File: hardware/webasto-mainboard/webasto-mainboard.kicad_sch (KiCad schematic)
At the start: 15 parts, among them J1 Console FTDI, J2 DEBUG, Q1 DMG2301L, U1 CY15E004J, U2 Pico, U3 LM4040DIM3-3.0

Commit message: Update title block on mainboard, print PDFs
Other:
- company: (none) -> Gavin Hurlbut
- title: Webasto Thermo Top C Replacement Controller -> Webasto Replacement Mainboard (Thermo Top C)
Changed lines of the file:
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@@
   (paper "A4")
   (title_block
-    (title "Webasto Thermo Top C Replacement Controller")
-    (date "2023-01-19")
+    (title "Webasto Replacement Mainboard (Thermo Top C)")
+    (date "2023-01-31")
     (rev "v1.0")
+    (company "Gavin Hurlbut")
   )
   (junction (at 122.301 114.173) (diameter 0) (color 0 0 0 0)

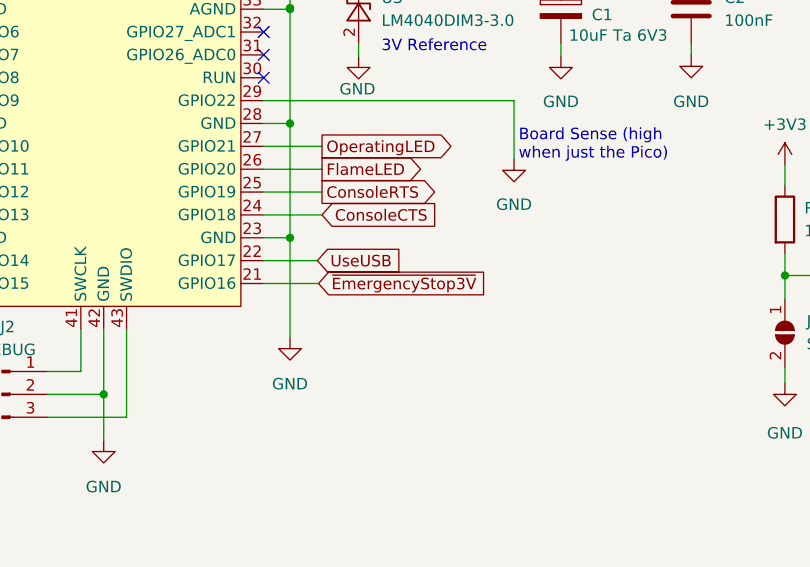
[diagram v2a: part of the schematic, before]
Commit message: Moved emerg. shutdown offboard
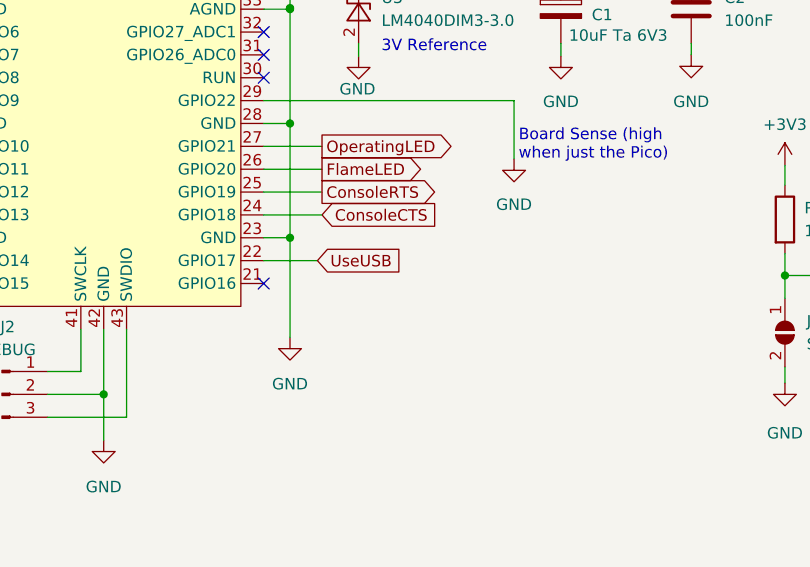
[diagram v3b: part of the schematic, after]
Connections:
- net ~{EmergencyStop3V}: no longer names the net of U2.21 (GPIO16)
- no-connect marks 5 -> 6

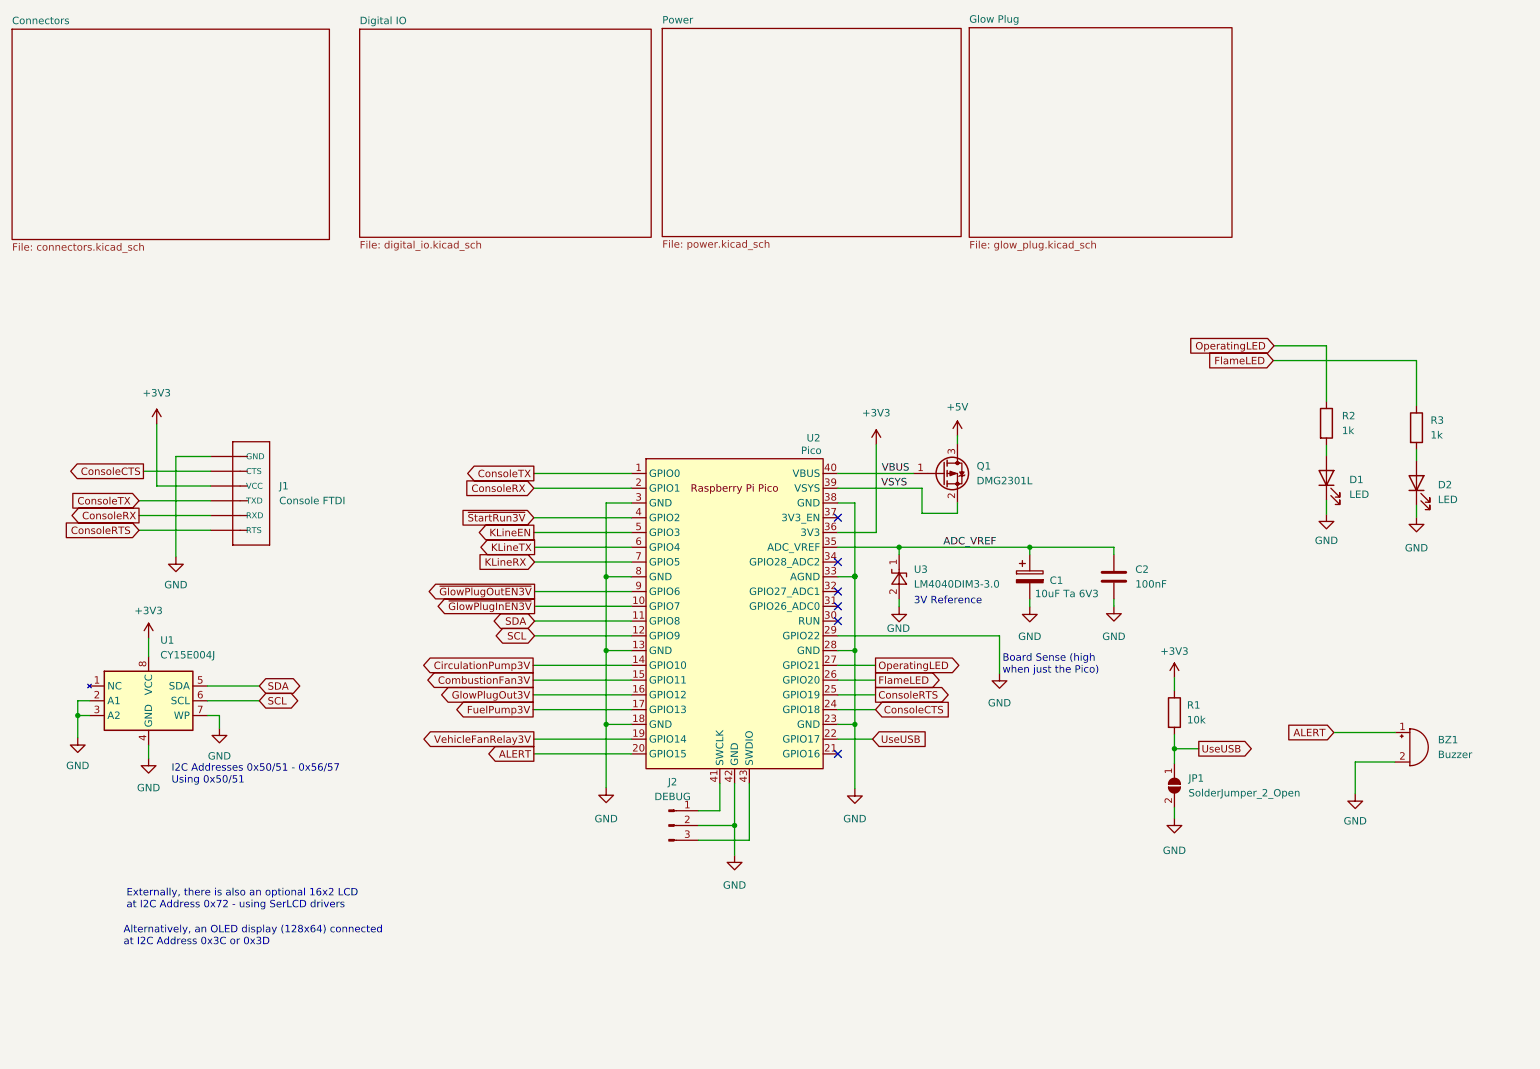
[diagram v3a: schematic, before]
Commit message: Got rid of TINY diode (0402!?!?), remove USE_USB, put in PicoW
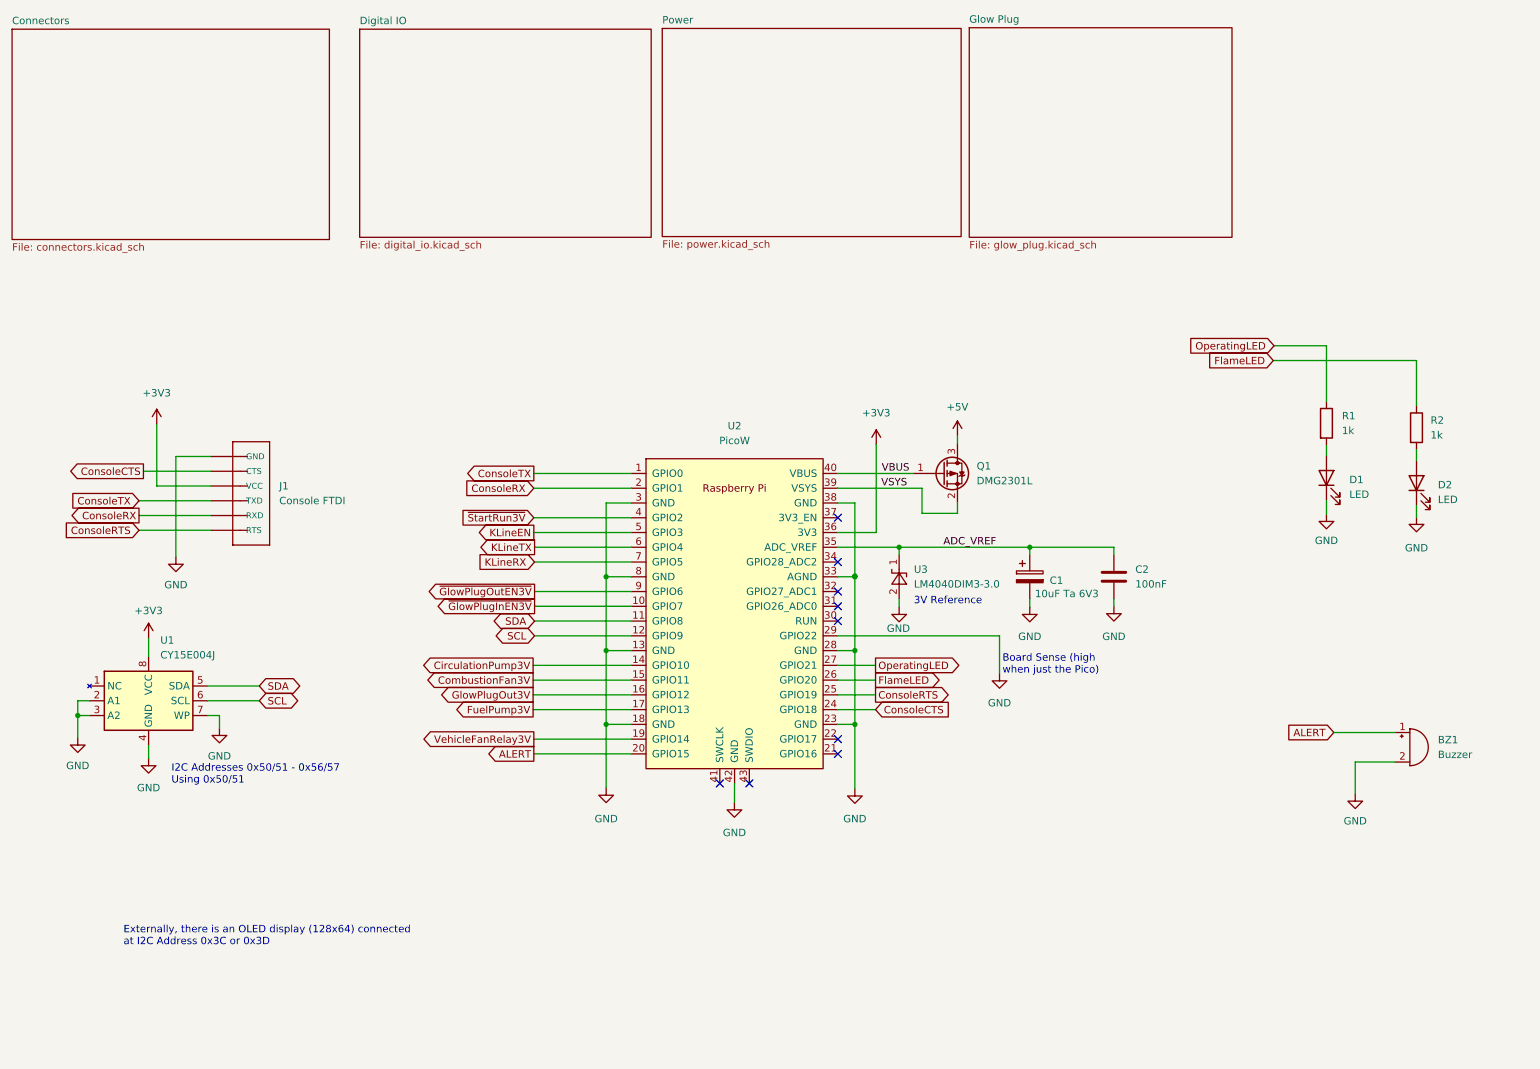
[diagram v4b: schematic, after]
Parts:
- removed J2: DEBUG, Connector_PinHeader_2.54mm:PinHeader_1x03_P2.54mm_Vertical, symbol Connector:Conn_01x03_Male
- removed JP1: SolderJumper_2_Open, Jumper:SolderJumper-2_P1.3mm_Open_TrianglePad1.0x1.5mm, symbol Jumper:SolderJumper_2_Open
- removed R1: 10k, Resistor_SMD:R_0805_2012Metric_Pad1.20x1.40mm_HandSolder, symbol Device:R
- removed U2: Pico, MCU_RaspberryPi_and_Boards:RPi_Pico_SMD_TH, symbol MCU_RaspberryPi_and_Boards:Pico
- added U2: PicoW, RPi_Pico:RPi_PicoW_SMD_TH, symbol RPi_Pico:PicoW
- renumbered R2 to R1, R3 to R2
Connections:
- net +3V3: now also U2.36 (3V3)
- net ADC_VREF: now also U2.35 (ADC_VREF)
- net ALERT: now also U2.20 (GPIO15)
- net CirculationPump3V: now also U2.14 (GPIO10)
- net CombustionFan3V: now also U2.15 (GPIO11)
- net ConsoleCTS: now also U2.24 (GPIO18)
- net ConsoleRTS: now also U2.25 (GPIO19)
- net ConsoleRX: now also U2.2 (GPIO1)
- net ConsoleTX: now also U2.1 (GPIO0)
- net FlameLED: now also U2.26 (GPIO20)
- net FuelPump3V: now also U2.17 (GPIO13)
- net GND: now also U2.13 (GND), U2.18 (GND), U2.23 (GND), U2.28 (GND), U2.29 (GPIO22), U2.3 (GND), U2.33 (AGND), U2.42 (GND), U2.8 (GND)
- net GlowPlugOut3V: now also U2.16 (GPIO12)
- net KLineEN: now also U2.5 (GPIO3)
- net KLineRX: now also U2.7 (GPIO5)
- net KLineTX: now also U2.6 (GPIO4)
- net OperatingLED: now also U2.27 (GPIO21)
- net SCL: now also U2.12 (GPIO9)
- net SDA: now also U2.11 (GPIO8)
- net VBUS: now also U2.40 (VBUS)
- net VSYS: now also U2.39 (VSYS)
- net VehicleFanRelay3V: now also U2.19 (GPIO14)
- net ~{GlowPlugInEN3V}: now also U2.10 (GPIO7)
- net ~{GlowPlugOutEN3V}: now also U2.9 (GPIO6)
- net ~{StartRun3V}: now also U2.4 (GPIO2)
- no-connect marks 6 -> 9
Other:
- note added: "Externally, there is an OLED display (128x64) connected at I2C Address 0x3C or 0x3D"
- note removed: "Alternatively, an OLED display (128x64) connected at I2C Address 0x3C or 0x3D"
- note removed: "Externally, there is also an optional 16x2 LCD at I2C Address 0x72 - using SerLCD drivers"

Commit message: Move VSYS to ADC2 to avoid the stupid WiFi setup
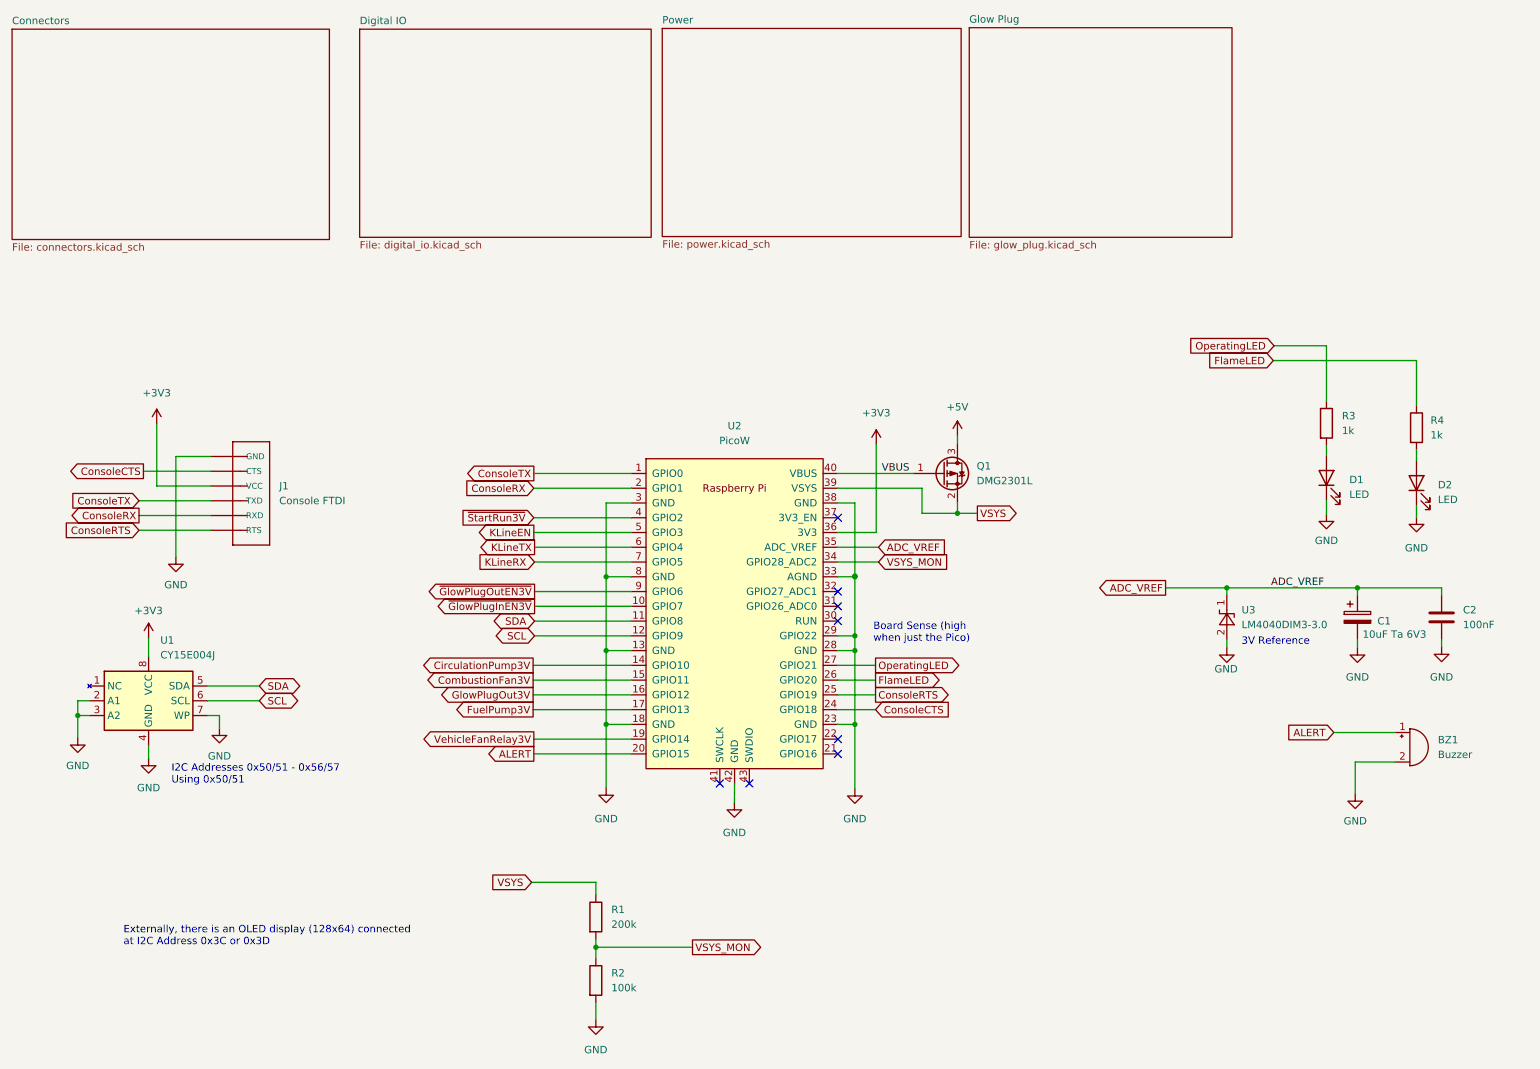
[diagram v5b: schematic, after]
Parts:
- added R1: 200k, Resistor_SMD:R_0805_2012Metric_Pad1.20x1.40mm_HandSolder, symbol Device:R
- added R2: 100k, Resistor_SMD:R_0805_2012Metric_Pad1.20x1.40mm_HandSolder, symbol Device:R
- renumbered R1 to R3, R2 to R4
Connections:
- net GND: now also R2.2
- net VSYS: now also R1.1
- net VSYS_MON: now reaches U2.34 (GPIO28_ADC2)
- net VSYS_MON: now also R1.2, R2.1
- no-connect marks 9 -> 8
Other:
- moved on the sheet: C1, C2, U3

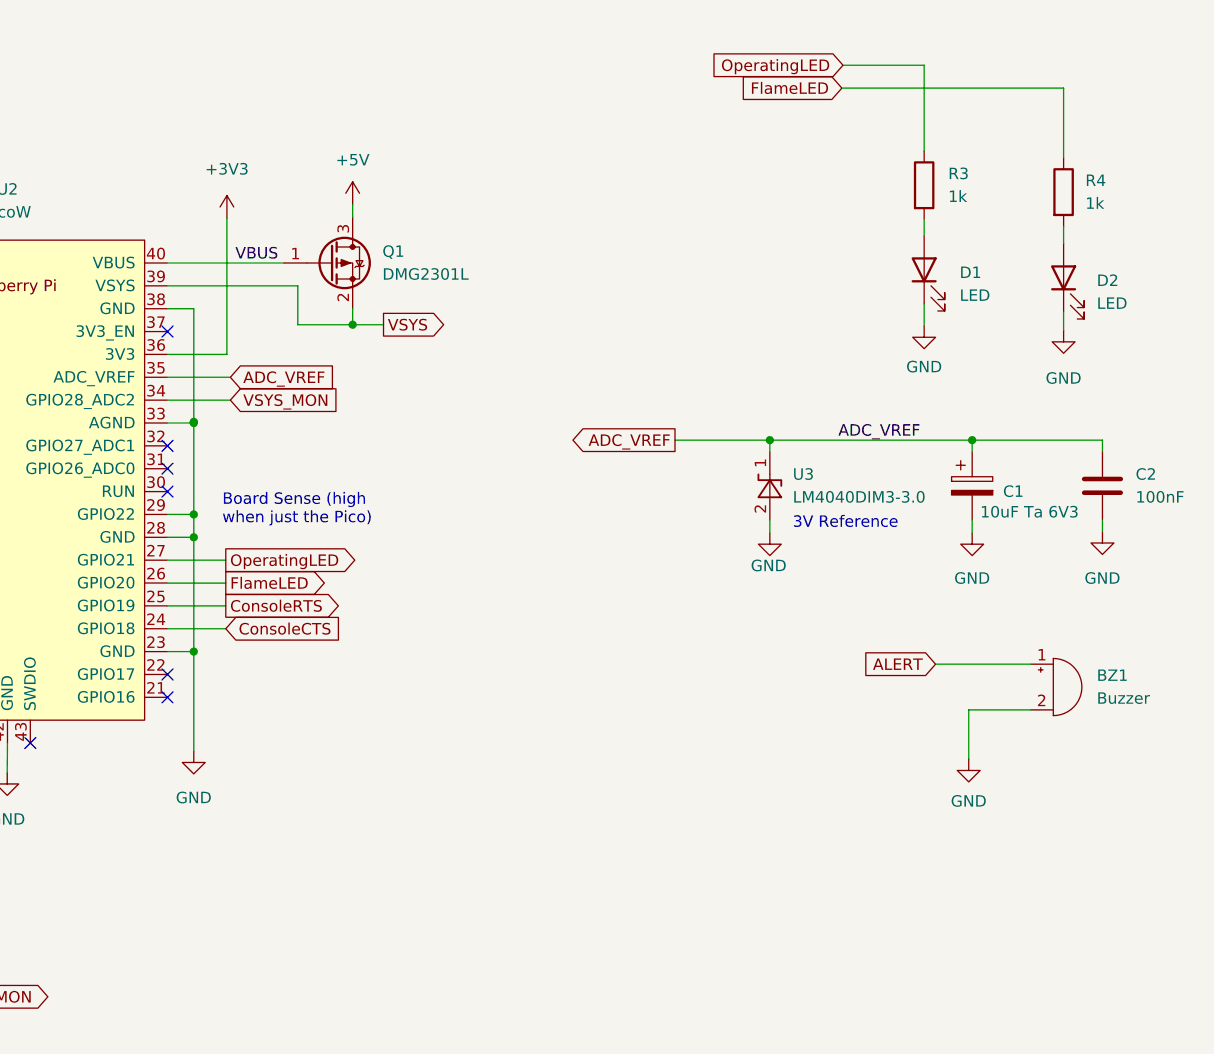
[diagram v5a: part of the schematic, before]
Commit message: Move the LED to the mainboard
- due to how the driver doesn't share the SPI bus well, you currently can
  either use the TCP stack or the GPIOs.  Mixing will cause weird crashes.
- so I'm adding the LED onto the mainboard directly.
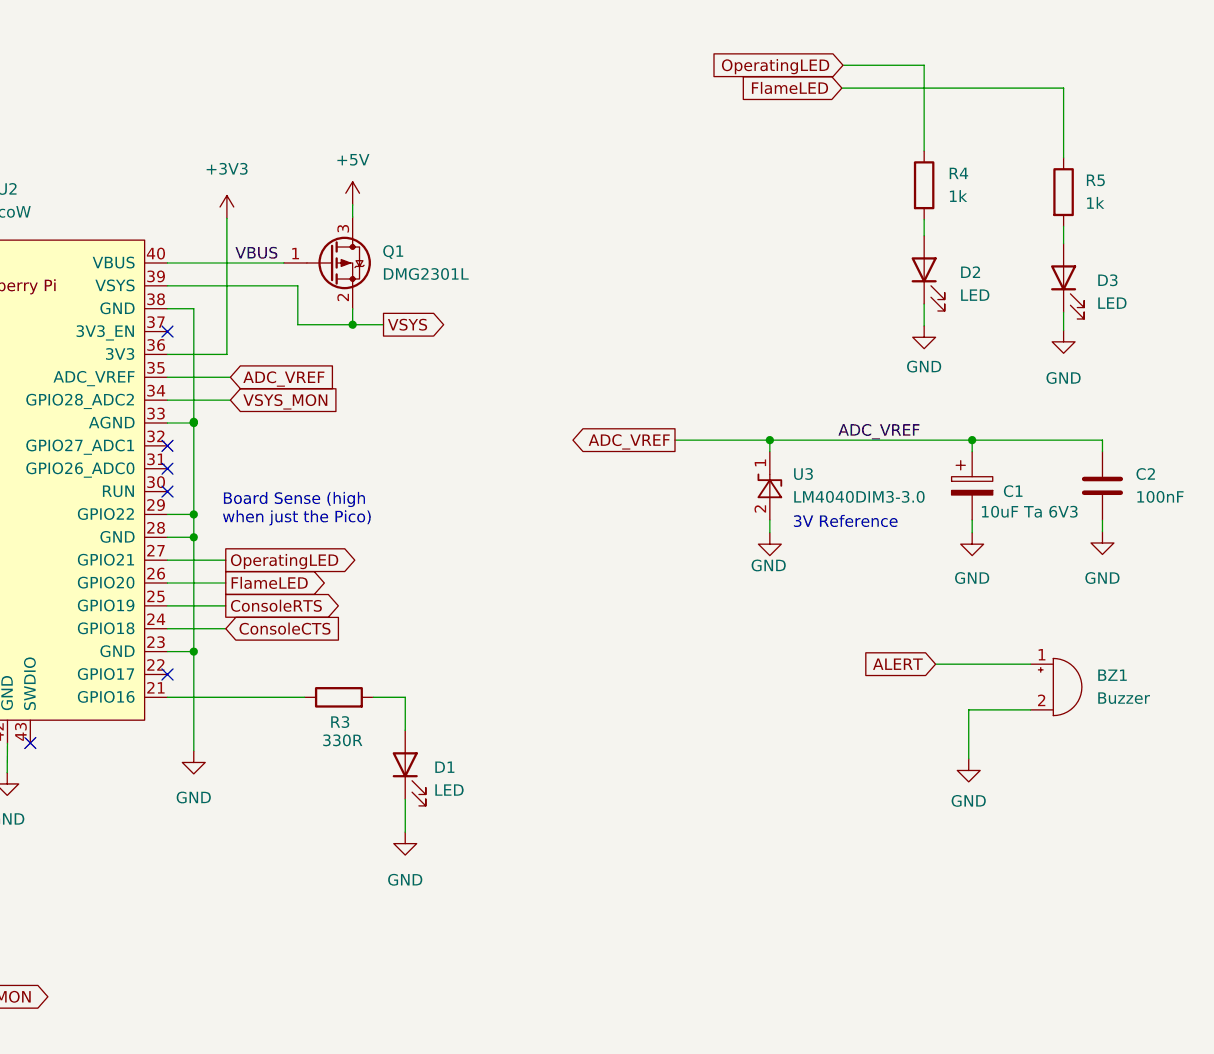
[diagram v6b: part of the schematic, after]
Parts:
- added D1: LED, LED_SMD:LED_0805_2012Metric_Pad1.15x1.40mm_HandSolder, symbol Device:LED
- added R3: 330R, Resistor_SMD:R_0805_2012Metric_Pad1.20x1.40mm_HandSolder, symbol Device:R
- renumbered D1 to D2, D2 to D3, R3 to R4, R4 to R5
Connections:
- net GND: now also D1.1 (K)
- net at U2.21 (GPIO16): now also R3.1
- new net: D1.2 (A), R3.2
- no-connect marks 8 -> 7
